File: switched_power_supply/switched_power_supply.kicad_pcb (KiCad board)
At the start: 2 copper layers, 80 x 80 mm, 36 parts, among them IC1 VIPER53ESPTR-E, T1 Transformador_1x2, U1 Viper53, U2 TL431, U3 PC817 Opto

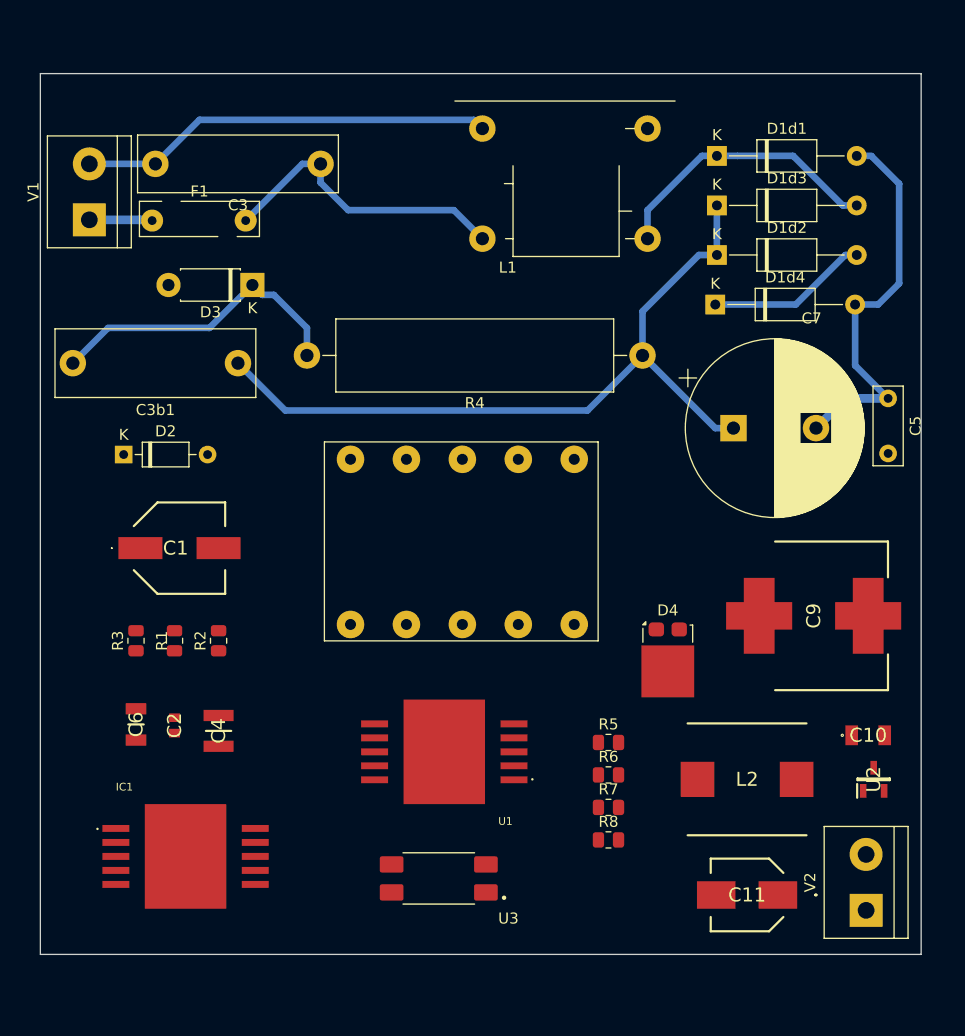
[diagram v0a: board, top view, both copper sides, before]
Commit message: footprint EMI ind. corrigido
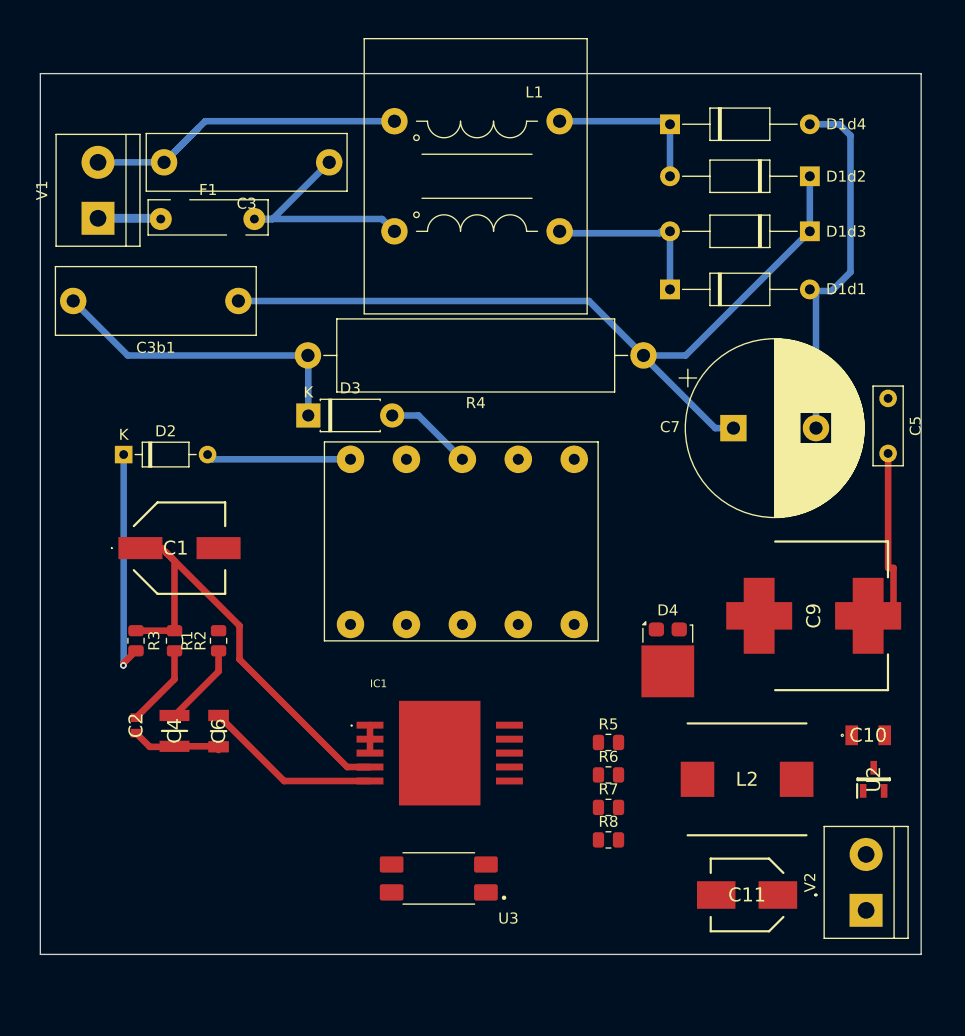
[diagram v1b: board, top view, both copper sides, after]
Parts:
- removed U1: Viper53, pci:SOIC127P1410X370-11N
- L1: value Indutor EMI -> SC-03-30J
- moved L1 25.3 mm to (139.0, 57.2), turned to 0 degrees
- moved IC1 24.9 mm to (143.1, 114.6)
- moved D1d4 16.9 mm to (164.0, 57.5)
- moved D3 12.9 mm to (131.2, 84.0), turned to 0 degrees
- moved D1d1 12.9 mm to (164.0, 72.5)
- moved D1d2 11.1 mm to (176.7, 62.2), turned to 180 degrees
- moved D1d3 8.76 mm to (176.7, 67.2), turned to 180 degrees
- moved C6 7.52 mm to (123.0, 112.6), turned to -90 degrees
- moved C3b1 5.65 mm to (124.8, 73.5)
- moved C4 4.00 mm to (119.0, 112.6), turned to -90 degrees
- moved C2 3.50 mm to (115.5, 112.1), turned to -90 degrees
- moved C3 0.80 mm to (133.1, 61.0)
- moved F1 0.80 mm to (119.5, 65.4)
- moved V1 0.80 mm to (112.0, 66.0)
- moved R4 0.09 mm to (161.6, 78.5)
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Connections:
- L1 pad 1: Net-(D1d1-K) -> Net-(C3-Pad2)
- L1 pad 2: Net-(C3-Pad1) -> Net-(D1d2-A)
- L1 pad 3: Net-(D1d2-A) -> Net-(C3-Pad1)
- L1 pad 4: Net-(C3-Pad2) -> Net-(D1d1-K)
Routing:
- net /Vdd: track 0.00 -> 41.8 mm
- net Net-(D2-K): track 0.00 -> 21.0 mm, vias 0 -> 1
- net Terra: track 0.00 -> 18.0 mm
- net /TOVL: track 0.00 -> 16.2 mm
- net Net-(D2-A): track 0.00 -> 13.2 mm
- net Net-(D1d1-K): track 25.5 -> 15.4 mm
- net /Drain: track 0.00 -> 8.02 mm
- net Net-(C4-Pad1): track 0.00 -> 7.53 mm
- net /Osc: track 0.00 -> 7.52 mm
- net /BarP: track 70.1 -> 75.8 mm
- net GND: track 36.8 -> 42.0 mm
- net Net-(C3-Pad2): track 37.7 -> 32.9 mm
- net Net-(C3-Pad1): track 27.4 -> 23.0 mm
- net Net-(IC1-NC_1): track 0.00 -> 2.54 mm
- net Net-(D1d2-A): track 14.7 -> 15.6 mm
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
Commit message: pcb atualizado
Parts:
- removed C1: Capacitor_Eletrolitico, pci:EEHZT1E331UP
- moved U2 46.5 mm to (136.0, 116.9), turned to 0 degrees
- moved C10 42.0 mm to (140.1, 115.5), turned to -90 degrees
- moved IC1 26.4 mm to (122.4, 98.3), turned to 180 degrees
- moved R6 25.8 mm to (132.8, 120.4), turned to 90 degrees
- moved R5 25.5 mm to (133.0, 114.9), turned to 90 degrees
- moved U3 24.8 mm to (122.5, 112.0), turned to 90 degrees
- moved C6 20.5 mm to (132.4, 94.4), turned to 90 degrees
- moved R8 18.4 mm to (140.1, 120.4), turned to -90 degrees
- moved R7 15.8 mm to (143.0, 116.0), turned to -90 degrees
- moved D3 12.7 mm to (118.7, 81.3)
- moved C2 12.0 mm to (111.2, 100.9)
- moved R2 11.8 mm to (111.2, 104.5)
- moved C11 11.1 mm to (173.0, 116.6), turned to 90 degrees
- moved R3 10.8 mm to (111.2, 94.5), turned to 90 degrees
- moved R1 10.1 mm to (111.2, 97.9)
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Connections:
- D4 pad 3: (no net) -> Net-(D4-A)
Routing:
- net GND: track 42.0 -> 145.1 mm
- net Terra: track 18.0 -> 113.0 mm, vias 0 -> 1
- net /Vout: track 0.00 -> 61.2 mm, vias 0 -> 1
- net Net-(D4-K): track 0.00 -> 52.6 mm
- net /Drain: track 8.02 -> 46.4 mm
- net /Cmp: track 0.00 -> 29.2 mm, vias 0 -> 2
- net Net-(U3-Cath): track 0.00 -> 21.3 mm
- net Net-(U3-Anode): track 0.00 -> 17.4 mm
- net /TOVL: track 16.2 -> 3.85 mm
- net /Vdd: track 41.8 -> 30.2 mm, vias 0 -> 2
- net Net-(D2-K): track 21.0 -> 10.5 mm, vias 1 -> 0
- net Net-(C10-Pad2): track 0.00 -> 8.45 mm
- net Net-(D4-A): track 0.00 -> 6.19 mm
- net Net-(C3-Pad2): track 32.9 -> 38.9 mm
- net /BarP: track 75.8 -> 81.3 mm
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- added copper zone on F.Cu, net GND
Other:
- board size 80 x 80 mm -> 80 x 75 mm

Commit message: Uploading files
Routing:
- net Terra: track 113.0 -> 112.3 mm
- net /Drain: track 46.4 -> 46.5 mm, vias 0 -> 1
- net Net-(D2-K): track 10.5 -> 10.6 mm, vias 0 -> 1
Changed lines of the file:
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@@
 			)
 		)
-		(pad "1" smd rect
+		(pad "" smd rect
+			(at -2.35 -4.95 270)
+			(size 2.2 2.8)
+			(layers "F.Cu" "F.Paste" "F.Mask")
+			(net 13 "Terra")
+			(pinfunction "2")
+			(pintype "passive")
+		)
+		(pad "" smd rect
 			(at -2.35 4.95 270)
 			(size 2.2 2.8)
@@
 			(pintype "passive")
 		)
-		(pad "1" smd rect
-			(at 0 4.95 270)
-			(size 2.5 6)
+		(pad "" smd rect
+			(at 2.35 -4.95 270)
+			(size 2.2 2.8)
 			(layers "F.Cu" "F.Paste" "F.Mask")
-			(net 19 "Net-(D4-K)")
-			(pinfunction "1")
+			(net 13 "Terra")
+			(pinfunction "2")
 			(pintype "passive")
 		)
-		(pad "1" smd rect
+		(pad "" smd rect
 			(at 2.35 4.95 270)
 			(size 2.2 2.8)
@@
 			(pintype "passive")
 		)
-		(pad "2" smd rect
-			(at -2.35 -4.95 270)
-			(size 2.2 2.8)
+		(pad "1" smd rect
+			(at 0 4.95 270)
+			(size 2.5 6)
 			(layers "F.Cu" "F.Paste" "F.Mask")
-			(net 13 "Terra")
-			(pinfunction "2")
+			(net 19 "Net-(D4-K)")
+			(pinfunction "1")
 			(pintype "passive")
 		)
@@
 			(pintype "passive")
 		)
-		(pad "2" smd rect
-			(at 2.35 -4.95 270)
-			(size 2.2 2.8)
-			(layers "F.Cu" "F.Paste" "F.Mask")
-			(net 13 "Terra")
-			(pinfunction "2")
-			(pintype "passive")
-		)
 		(model "${KIPRJMOD}/footprints/cap_1.2mf_saida/EEE-FK1E122SV/3D/EEE-FK1E122SV.stp"
 			(offset
@@
 		)
 		(property "Value" "TL431"
-			(at 0 0 360)
+			(at 0 0 0)
 			(layer "F.SilkS")
 			(hide yes)
@@
 		)
 		(property "Footprint" "pci:SOT95P237X112-3N"
-			(at 0 0 360)
+			(at 0 0 0)
 			(layer "F.Fab")
 			(hide yes)
@@
 		)
 		(property "Datasheet" ""
-			(at 0 0 360)
+			(at 0 0 0)
 			(layer "F.Fab")
 			(hide yes)
@@
 		)
 		(property "Description" "Triac"
-			(at 0 0 360)
+			(at 0 0 0)
 			(layer "F.Fab")
 			(hide yes)
@@
 		)
 		(fp_text user "${REFERENCE}"
-			(at 0 0 360)
+			(at 0 0 0)
 			(layer "F.Fab")
 			(effects
@@
 		)
 		(property "Value" "Resistor SMD"
-			(at -11.5525 -5.42 360)
+			(at -11.5525 -5.42 0)
 			(layer "F.Fab")
 			(hide yes)
@@
 		)
 		(property "Value" "VIPER53ESPTR-E"
-			(at -0.1625 0 360)
+			(at -0.1625 0 0)
 			(layer "F.Fab")
 			(effects
@@
 		)
 		(property "Footprint" "pci:SOIC127P1410X370-11N"
-			(at 0 0 360)
+			(at 0 0 0)
 			(layer "F.Fab")
 			(hide yes)
@@
 		)
 		(property "Datasheet" "https://www.st.com/resource/en/datasheet/viper53e-e.pdf"
-			(at 0 0 360)
+			(at 0 0 0)
 			(layer "F.Fab")
 			(hide yes)
@@
 		)
 		(property "Description" "Fixed frequency off line converter"
-			(at 0 0 360)
+			(at 0 0 0)
 			(layer "F.Fab")
 			(hide yes)
@@
 			(layer "F.Fab")
 		)
-		(fp_text user "K"
-			(at 0 -1.8 0)
-			(layer "F.SilkS")
-			(effects
-				(font
-					(size 1 1)
-					(thickness 0.15)
-				)
-			)
-		)
-		(fp_text user "K"
-			(at 0 -1.8 0)
-			(layer "F.Fab")
-			(effects
-				(font
-					(size 1 1)
-					(thickness 0.15)
-				)
-			)
-		)
 		(fp_text user "${REFERENCE}"
 			(at 4.11 0 0)
@@
 		)
 		(property "Value" "Resistor PTH"
-			(at -6.4225 1.44 360)
+			(at -6.4225 1.44 0)
 			(layer "F.Fab")
 			(hide yes)
@@
 	)
 	(segment
+		(start 135.0662 90.3)
+		(end 132.4228 92.9434)
+		(width 0.6)
+		(layer "F.Cu")
+		(net 2)
+	)
+	(segment
 		(start 123.8023 107.72)
 		(end 124.850257 107.72)
@@
 	)
 	(segment
-		(start 146.304 84.8885)
-		(end 138.2491 92.9434)
+		(start 140.8925 90.3)
+		(end 135.0662 90.3)
 		(width 0.6)
 		(layer "F.Cu")
@@
 	)
 	(segment
+		(start 146.304 84.8885)
+		(end 140.8925 90.3)
+		(width 0.6)
+		(layer "F.Cu")
+		(net 2)
+	)
+	(segment
 		(start 115.745 109.695)
 		(end 122.271846 109.695)
@@
 	)
 	(segment
-		(start 138.2491 92.9434)
-		(end 132.4228 92.9434)
-		(width 0.6)
-		(layer "F.Cu")
-		(net 2)
-	)
-	(segment
 		(start 177.2625 85.1)
 		(end 173.48 88.8825)
@@
 	)
 	(segment
-		(start 122.3698 85.2752)
-		(end 122.3698 89.6112)
+		(start 122.4 92)
+		(end 122.4 98.2932)
 		(width 0.6)
 		(layer "F.Cu")
@@
 	)
 	(segment
-		(start 122.3698 88.4374)
+		(start 122.4 98.2932)
 		(end 122.3698 98.3234)
 		(width 0.6)
@@
 		(net 6)
 	)
+	(via
+		(at 122.4 92)
+		(size 0.6)
+		(drill 0.3)
+		(layers "F.Cu" "B.Cu")
+		(net 6)
+	)
 	(segment
-		(start 126.365 81.28)
-		(end 122.3698 85.2752)
+		(start 122.4 83.1)
+		(end 122.4 92)
 		(width 0.6)
-		(layer "F.Cu")
+		(layer "B.Cu")
+		(net 6)
+	)
+	(segment
+		(start 124.22 81.28)
+		(end 122.4 83.1)
+		(width 0.6)
+		(layer "B.Cu")
 		(net 6)
 	)
@@
 	)
 	(segment
+		(start 126.365 81.28)
+		(end 124.22 81.28)
+		(width 0.6)
+		(layer "B.Cu")
+		(net 6)
+	)
+	(segment
 		(start 111.2138 103.6339)
 		(end 110.1743 103.6339)
@@
 	)
 	(segment
-		(start 143.070274 118.825)
-		(end 141.021774 120.8735)
+		(start 137.977 120.8735)
+		(end 134.9745 117.871)
 		(width 0.6)
 		(layer "F.Cu")
@@
 	)
 	(segment
-		(start 182.245 114.427)
-		(end 173.615 114.427)
-		(width 0.8)
+		(start 149.4 118.825)
+		(end 143.070274 118.825)
+		(width 0.6)
 		(layer "F.Cu")
 		(net 13)
 	)
 	(segment
-		(start 155.3598 112.8652)
-		(end 149.4 118.825)
-		(width 0.6)
+		(start 182.245 114.427)
+		(end 173.615 114.427)
+		(width 0.8)
 		(layer "F.Cu")
 		(net 13)
 	)
 	(segment
-		(start 155.3598 112.8402)
-		(end 155.3598 112.8652)
+		(start 141.021774 120.8735)
+		(end 137.977 120.8735)
 		(width 0.6)
 		(layer "F.Cu")
@@
 	)
 	(segment
-		(start 149.4 118.825)
-		(end 143.070274 118.825)
-		(width 0.6)
-		(layer "F.Cu")
-		(net 13)
-	)
-	(segment
 		(start 134.9745 117.871)
 		(end 138.3895 121.286)
@@
 	)
 	(segment
-		(start 141.021774 120.8735)
-		(end 137.977 120.8735)
-		(width 0.6)
-		(layer "F.Cu")
-		(net 13)
-	)
-	(segment
 		(start 182.245 102.395)
 		(end 182.245 113.937)
@@
 	)
 	(segment
-		(start 137.977 120.8735)
-		(end 134.9745 117.871)
+		(start 154.7625 113.4625)
+		(end 149.4 118.825)
 		(width 0.6)
 		(layer "F.Cu")
@@
 		(net 13)
 	)
+	(segment
+		(start 143.070274 118.825)
+		(end 141.021774 120.8735)
+		(width 0.6)
+		(layer "F.Cu")
+		(net 13)
+	)
 	(via
-		(at 155.3598 112.8402)
+		(at 154.7625 113.4625)
 		(size 0.6)
 		(drill 0.3)
@@
 	(segment
 		(start 182.245 114.427)
-		(end 156.9466 114.427)
+		(end 155.627 114.427)
 		(width 0.8)
 		(layer "B.Cu")
@@
 	)
 	(segment
-		(start 142.4081 99.8885)
-		(end 141.224 99.8885)
+		(start 155.627 114.427)
+		(end 141.224 100.024)
 		(width 0.8)
 		(layer "B.Cu")
@@
 	)
 	(segment
-		(start 156.9466 114.427)
-		(end 142.4081 99.8885)
+		(start 141.224 100.024)
+		(end 141.224 99.8885)
 		(width 0.8)
 		(layer "B.Cu")
@@
 	(segment
 		(start 111.2138 93.6244)
-		(end 111.4178 93.6244)
+		(end 111.2256 93.6244)
 		(width 0.6)
 		(layer "F.Cu")
@@
 	)
 	(segment
-		(start 111.4178 93.6244)
-		(end 118.6822 86.36)
+		(start 111.2256 93.6244)
+		(end 112.9 91.95)
 		(width 0.6)
 		(layer "F.Cu")
@@
 		(net 16)
 	)
+	(via
+		(at 112.9 91.95)
+		(size 0.6)
+		(drill 0.3)
+		(layers "F.Cu" "B.Cu")
+		(net 16)
+	)
+	(segment
+		(start 118.49 86.36)
+		(end 118.745 86.36)
+		(width 0.6)
+		(layer "B.Cu")
+		(net 16)
+	)
+	(segment
+		(start 112.9 91.95)
+		(end 118.49 86.36)
+		(width 0.6)
+		(layer "B.Cu")
+		(net 16)
+	)
 	(segment
 		(start 137.86 66.11)
@@
 	)
 	(segment
-		(start 147.7213 115.1176)
-		(end 153.0652 115.1176)
+		(start 147.7213 115.2213)
+		(end 152.007 119.507)
 		(width 0.8)
 		(layer "B.Cu")
@@
 	)
 	(segment
-		(start 153.0652 115.1176)
-		(end 157.4546 119.507)
+		(start 152.007 119.507)
+		(end 182.245 119.507)
 		(width 0.8)
 		(layer "B.Cu")
@@
 	)
 	(segment
-		(start 157.4546 119.507)
-		(end 182.245 119.507)
+		(start 147.7213 115.1176)
+		(end 147.7213 115.2213)
 		(width 0.8)
 		(layer "B.Cu")
@@
 		(polygon
 			(pts
-				(xy 108 91.025) (xy 136.975 91.025) (xy 136.975 98.025) (xy 125.025 109.975) (xy 109.825 109.975)
-				(xy 107.975 108.125) (xy 107.975 91.025) (xy 108.175 91.025) (xy 108.2 91.05) (xy 108.025 91.05)
+				(xy 107.5 92) (xy 110 90) (xy 136 90) (xy 136 101.2) (xy 127 110) (xy 112 110) (xy 107.5 106)
 			)
 		)

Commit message: quase pronto
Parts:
- added REF**: Fiducial_1.5mm_Mask3mm, Fiducial:Fiducial_1.5mm_Mask3mm, F.Cu at (112.0, 113.5)
- added REF**: Fiducial_1.5mm_Mask3mm, Fiducial:Fiducial_1.5mm_Mask3mm, F.Cu at (117.0, 51.5)
- added REF**: Fiducial_1.5mm_Mask3mm, Fiducial:Fiducial_1.5mm_Mask3mm, F.Cu at (181.5, 52.5)
- moved C5 13.7 mm to (174.5, 92.5), turned to 0 degrees
- moved C7 4.54 mm to (173.5, 82.5)
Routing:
- net Terra: track 112.3 -> 98.3 mm
- net Net-(D4-K): track 52.6 -> 55.3 mm, vias 0 -> 2
- net /Drain: track 46.5 -> 48.3 mm
- net /BarP: track 81.3 -> 80.0 mm
- net GND: track 145.1 -> 145.6 mm
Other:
- board size 80 x 75 mm -> 80 x 80 mm
- board text added: "127-220V ~ 60Hz"
- board text added: "12VDC @ 2A"
- board text added: "IFSC"
- board text added: "IN"
- board text added: "Isolated Flyback Converter"
- board text added: "Murillo R. Fabricio S. PCI20307 2024.2"
- board text added: "OUT"
- board text added: "adicionar rasgo de isolamento ou espacamento de 8mm furo pra fixar deixar trilhas com 2.5mm de distancia no primario"

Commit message: Realizando correções...
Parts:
- added REF**: MountingHole_3.2mm_M3_ISO14580, MountingHole:MountingHole_3.2mm_M3_ISO14580, F.Cu at (183.0, 125.5)
- added REF**: MountingHole_3.2mm_M3_ISO14580, MountingHole:MountingHole_3.2mm_M3_ISO14580, F.Cu at (110.5, 125.5)
- added REF**: MountingHole_3.2mm_M3_ISO14580, MountingHole:MountingHole_3.2mm_M3_ISO14580, F.Cu at (110.5, 53.0)
- added REF**: MountingHole_3.2mm_M3_ISO14580, MountingHole:MountingHole_3.2mm_M3_ISO14580, F.Cu at (183.0, 53.0)
- moved REF** 6.18 mm to (175.5, 54.0)
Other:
- outline, holes or cut-outs redrawn
- board text removed: "OUT"
